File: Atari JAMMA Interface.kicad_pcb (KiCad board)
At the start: 2 copper layers, 112.2 x 74.8 mm, 45 parts, among them P1 10K, U1 LM386, U2 DIP-14_W7.62mm, U3 MC34063AP, U4 74LS04

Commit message: minor tweaks to inductor
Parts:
- moved L1 0.09 mm to (109.6, 125.6)
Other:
- board text added: "1A"
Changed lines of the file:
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@@
 	(footprint "Inductor_THT:L_Radial_D6.0mm_P4.00mm"
 		(layer "F.Cu")
-		(at 109.6 125.5)
+		(at 109.6 125.59)
 		(descr "Inductor, Radial series, Radial, pin pitch=4.00mm, diameter=6.0mm, height=4.6mm, http://www.abracon.com/Magnetics/radial/AIUR-07.pdf")
 		(tags "Inductor Radial series Radial pin pitch 4.00mm  diameter 6.0mm height 4.6mm")
@@
 		)
 	)
+	(gr_text "1A"
+		(at 111.6 131.275538 0)
+		(layer "F.SilkS")
+		(effects
+			(font
+				(size 0.72 0.72)
+				(thickness 0.108)
+			)
+		)
+	)
 	(gr_text "1P B4"
 		(at 120.191885 91.8 90)
@@
 	)
 	(segment
-		(start 111 125.987872)
-		(end 111 114.2)
-		(width 0.2)
-		(layer "F.Cu")
-		(net 9)
-	)
-	(segment
-		(start 192.4 134.4)
-		(end 119.412128 134.4)
-		(width 0.2)
-		(layer "F.Cu")
-		(net 9)
-	)
-	(segment
-		(start 113.6 99.565685)
-		(end 113.6 98.8)
+		(start 115.8 96.6)
+		(end 115.8 93.4)
 		(width 0.2)
 		(layer "F.Cu")
@@
 	)
 	(segment
-		(start 176.82 122.58)
-		(end 179.59 125.35)
+		(start 108.4 111.6)
+		(end 108.4 104.765686)
 		(width 0.2)
 		(layer "F.Cu")
@@
 	)
 	(segment
-		(start 108.4 111.6)
-		(end 108.4 104.765686)
+		(start 176.82 122.58)
+		(end 179.59 125.35)
 		(width 0.2)
 		(layer "F.Cu")
@@
 	)
 	(segment
-		(start 116.4 92.8)
-		(end 122.430112 92.8)
+		(start 122.430112 92.8)
+		(end 128.428249 86.801863)
 		(width 0.2)
 		(layer "F.Cu")
@@
 	)
 	(segment
-		(start 113.6 98.8)
-		(end 115.8 96.6)
+		(start 113.6 99.565685)
+		(end 113.6 98.8)
 		(width 0.2)
 		(layer "F.Cu")
@@
 	)
 	(segment
-		(start 108.4 104.765686)
-		(end 113.6 99.565685)
+		(start 111 126.365685)
+		(end 111 114.2)
 		(width 0.2)
 		(layer "F.Cu")
@@
 	)
 	(segment
+		(start 113.6 98.8)
+		(end 115.8 96.6)
+		(width 0.2)
+		(layer "F.Cu")
+		(net 9)
+	)
+	(segment
+		(start 192.4 134.4)
+		(end 119.034314 134.4)
+		(width 0.2)
+		(layer "F.Cu")
+		(net 9)
+	)
+	(segment
 		(start 192.682856 134.4)
 		(end 197.282856 129.8)
@@
 	)
 	(segment
-		(start 128.428249 86.801863)
-		(end 128.428249 69.766603)
+		(start 116.4 92.8)
+		(end 122.430112 92.8)
 		(width 0.2)
 		(layer "F.Cu")
@@
 	)
 	(segment
-		(start 115.8 96.6)
-		(end 115.8 93.4)
+		(start 108.4 104.765686)
+		(end 113.6 99.565685)
 		(width 0.2)
 		(layer "F.Cu")
@@
 	)
 	(segment
-		(start 122.430112 92.8)
-		(end 128.428249 86.801863)
+		(start 128.428249 86.801863)
+		(end 128.428249 69.766603)
 		(width 0.2)
 		(layer "F.Cu")
@@
 	)
 	(segment
-		(start 119.412128 134.4)
-		(end 111 125.987872)
+		(start 119.034314 134.4)
+		(end 111 126.365685)
 		(width 0.2)
 		(layer "F.Cu")
@@
 	)
 	(segment
-		(start 111.6 121.6)
-		(end 111.6 126)
+		(start 111.6 117.2)
+		(end 111.54088 117.25912)
 		(width 0.2)
 		(layer "F.Cu")
@@
 	)
 	(segment
-		(start 131.898249 69.276603)
-		(end 131.898249 73.176603)
+		(start 166.95 134)
+		(end 167.2 133.75)
 		(width 0.2)
 		(layer "F.Cu")
@@
 	)
 	(segment
-		(start 193.2 129.8)
-		(end 193.454285 129.8)
+		(start 131.898249 69.276603)
+		(end 131.898249 73.176603)
 		(width 0.2)
 		(layer "F.Cu")
@@
 	)
 	(segment
-		(start 111.54088 121.54088)
-		(end 111.6 121.6)
+		(start 193.2 129.8)
+		(end 193.454285 129.8)
 		(width 0.2)
 		(layer "F.Cu")
@@
 	)
 	(segment
-		(start 119.6 134)
-		(end 166.95 134)
-		(width 0.2)
-		(layer "F.Cu")
-		(net 10)
-	)
-	(segment
-		(start 111.6 126)
-		(end 119.6 134)
+		(start 111.54088 121.54088)
+		(end 111.6 121.6)
 		(width 0.2)
 		(layer "F.Cu")
@@
 	)
 	(segment
+		(start 131.898249 73.176603)
+		(end 130.628249 74.446603)
+		(width 0.2)
+		(layer "F.Cu")
+		(net 10)
+	)
+	(segment
 		(start 111.54088 117.25912)
 		(end 111.54088 121.54088)
@@
 	)
 	(segment
-		(start 131.898249 73.176603)
-		(end 130.628249 74.446603)
+		(start 119.2 134)
+		(end 166.95 134)
 		(width 0.2)
 		(layer "F.Cu")
@@
 	)
 	(segment
-		(start 112.2 109.2)
-		(end 111.6 109.2)
+		(start 111.6 121.6)
+		(end 111.6 126.4)
 		(width 0.2)
 		(layer "F.Cu")
@@
 	)
 	(segment
-		(start 111.6 117.2)
-		(end 111.54088 117.25912)
+		(start 112.2 109.2)
+		(end 111.6 109.2)
 		(width 0.2)
 		(layer "F.Cu")
@@
 	)
 	(segment
-		(start 191.2 131.8)
-		(end 193.2 129.8)
+		(start 111.6 126.4)
+		(end 119.2 134)
 		(width 0.2)
 		(layer "F.Cu")
@@
 	)
 	(segment
-		(start 166.95 134)
-		(end 167.2 133.75)
+		(start 191.2 131.8)
+		(end 193.2 129.8)
 		(width 0.2)
 		(layer "F.Cu")
@@
 	)
 	(segment
-		(start 168.033704 133)
-		(end 167 133)
+		(start 119.4 133.6)
+		(end 112.2 126.4)
 		(width 0.2)
 		(layer "F.Cu")
@@
 	)
 	(segment
-		(start 167 133)
-		(end 166.4 133.6)
-		(width 0.2)
-		(layer "F.Cu")
-		(net 11)
-	)
-	(segment
-		(start 112.2 126)
-		(end 112.2 117.75912)
+		(start 112.2 117.75912)
+		(end 112.19088 117.75)
 		(width 0.2)
 		(layer "F.Cu")
@@
 	)
 	(segment
-		(start 166.4 133.6)
-		(end 119.8 133.6)
-		(width 0.2)
-		(layer "F.Cu")
-		(net 11)
-	)
-	(segment
-		(start 119.8 133.6)
-		(end 112.2 126)
+		(start 168.033704 133)
+		(end 167 133)
 		(width 0.2)
 		(layer "F.Cu")
@@
 	)
 	(segment
-		(start 112.2 117.75912)
-		(end 112.19088 117.75)
+		(start 112.2 126.4)
+		(end 112.2 117.75912)
 		(width 0.2)
 		(layer "F.Cu")
@@
 	)
 	(segment
+		(start 166.4 133.6)
+		(end 119.4 133.6)
+		(width 0.2)
+		(layer "F.Cu")
+		(net 11)
+	)
+	(segment
 		(start 187.8 131.4)
 		(end 189.4 129.8)
@@
 	)
 	(segment
+		(start 167 133)
+		(end 166.4 133.6)
+		(width 0.2)
+		(layer "F.Cu")
+		(net 11)
+	)
+	(segment
 		(start 174.28 130.2)
 		(end 175.48 131.4)
@@
 	)
 	(segment
-		(start 115.95 123.25)
-		(end 113.7 125.5)
-		(width 0.6)
-		(layer "F.Cu")
-		(net 52)
-	)
-	(segment
-		(start 126 128.960108)
-		(end 120.289892 123.25)
+		(start 126 130)
+		(end 126 128.4)
 		(width 0.6)
 		(layer "F.Cu")
@@
 	)
 	(segment
-		(start 126 130)
-		(end 126 128.960108)
+		(start 113.7 125.5)
+		(end 113.6 125.5)
 		(width 0.6)
 		(layer "F.Cu")
@@
 	)
 	(segment
-		(start 113.7 125.5)
-		(end 113.6 125.5)
+		(start 120.85 123.25)
+		(end 115.95 123.25)
 		(width 0.6)
 		(layer "F.Cu")
@@
 	)
 	(segment
-		(start 120.289892 123.25)
-		(end 115.95 123.25)
+		(start 126 128.4)
+		(end 120.85 123.25)
 		(width 0.6)
 		(layer "F.Cu")
@@
 		(width 0.6)
 		(layer "F.Cu")
+		(net 52)
+	)
+	(segment
+		(start 115.95 123.25)
+		(end 113.7 125.5)
+		(width 0.6)
+		(layer "F.Cu")

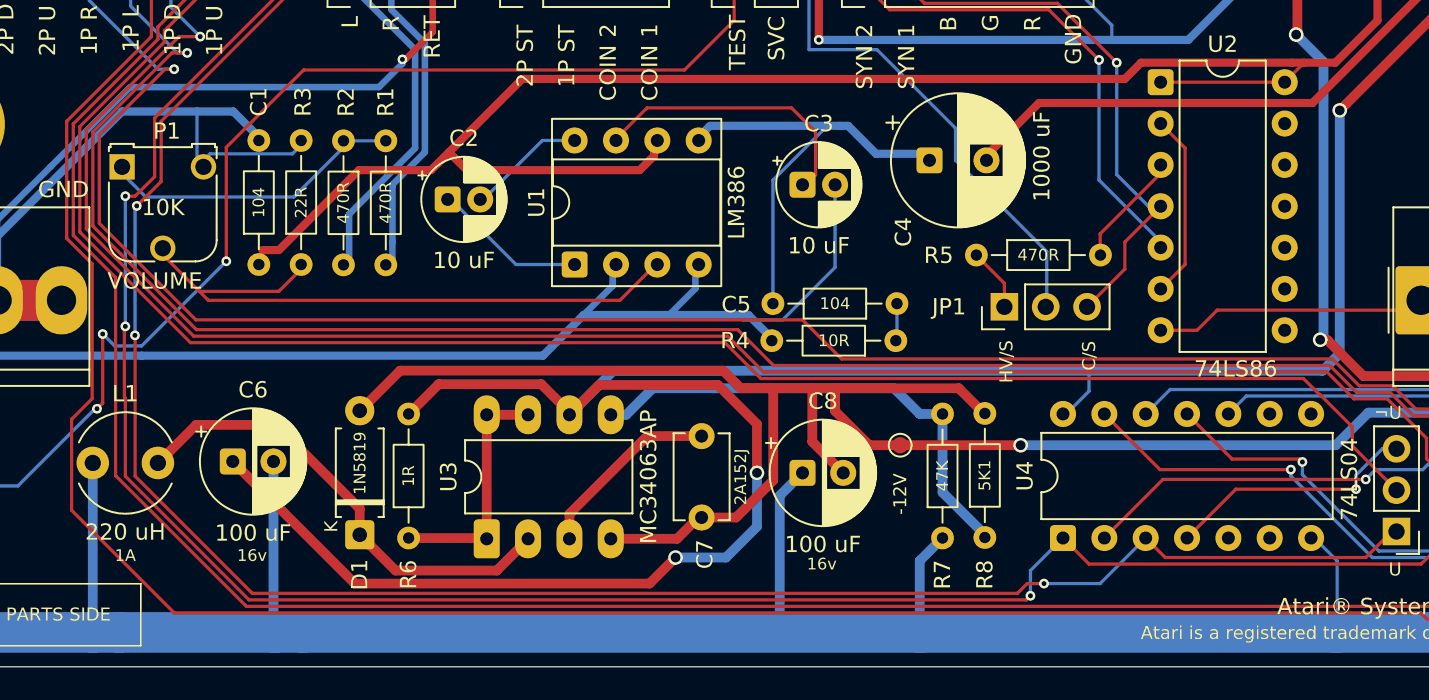
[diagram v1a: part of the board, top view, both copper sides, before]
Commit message: slight tweaks to layout and silkscreen
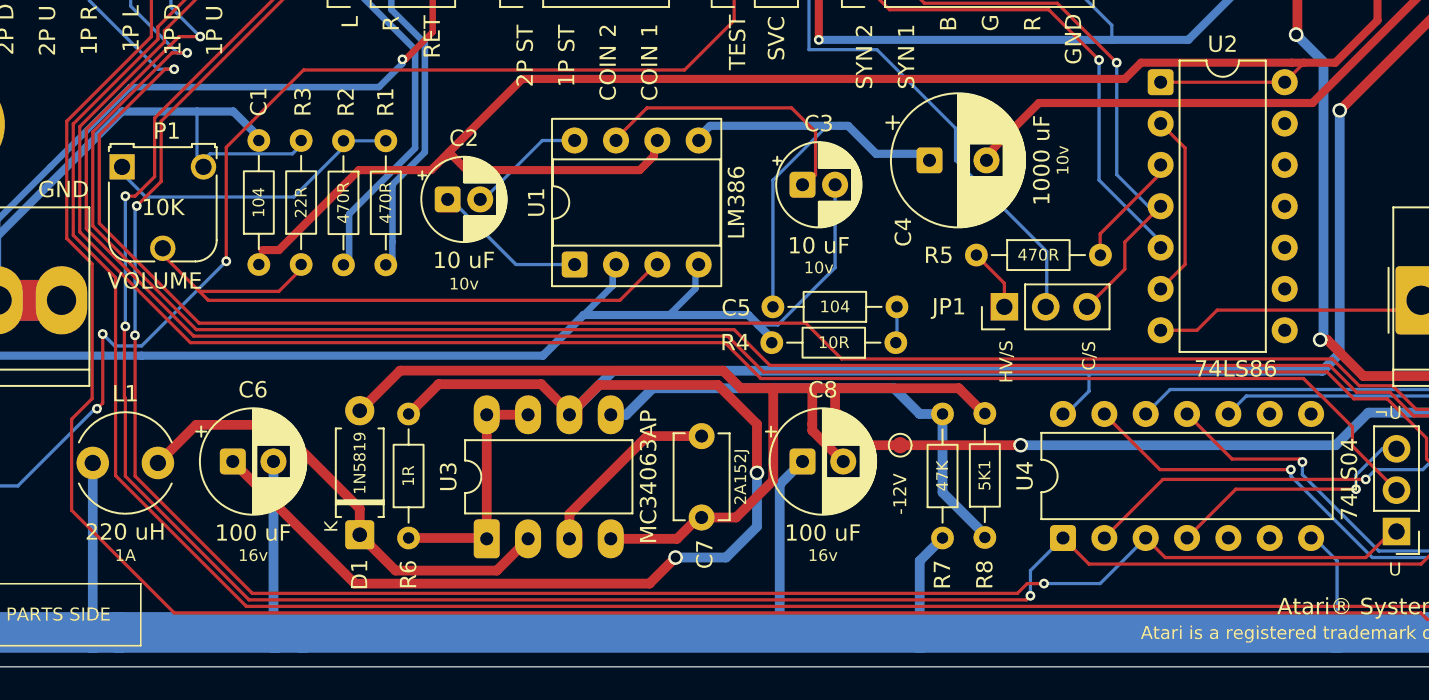
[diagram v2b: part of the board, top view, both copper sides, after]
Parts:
- moved C8 0.70 mm to (153.2, 125.5)
- moved C5 0.20 mm to (159.0, 116.0)
- moved R4 0.12 mm to (158.9, 118.2)
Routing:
- net -12V: track 151.6 -> 150.9 mm
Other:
- board text added: "10v"

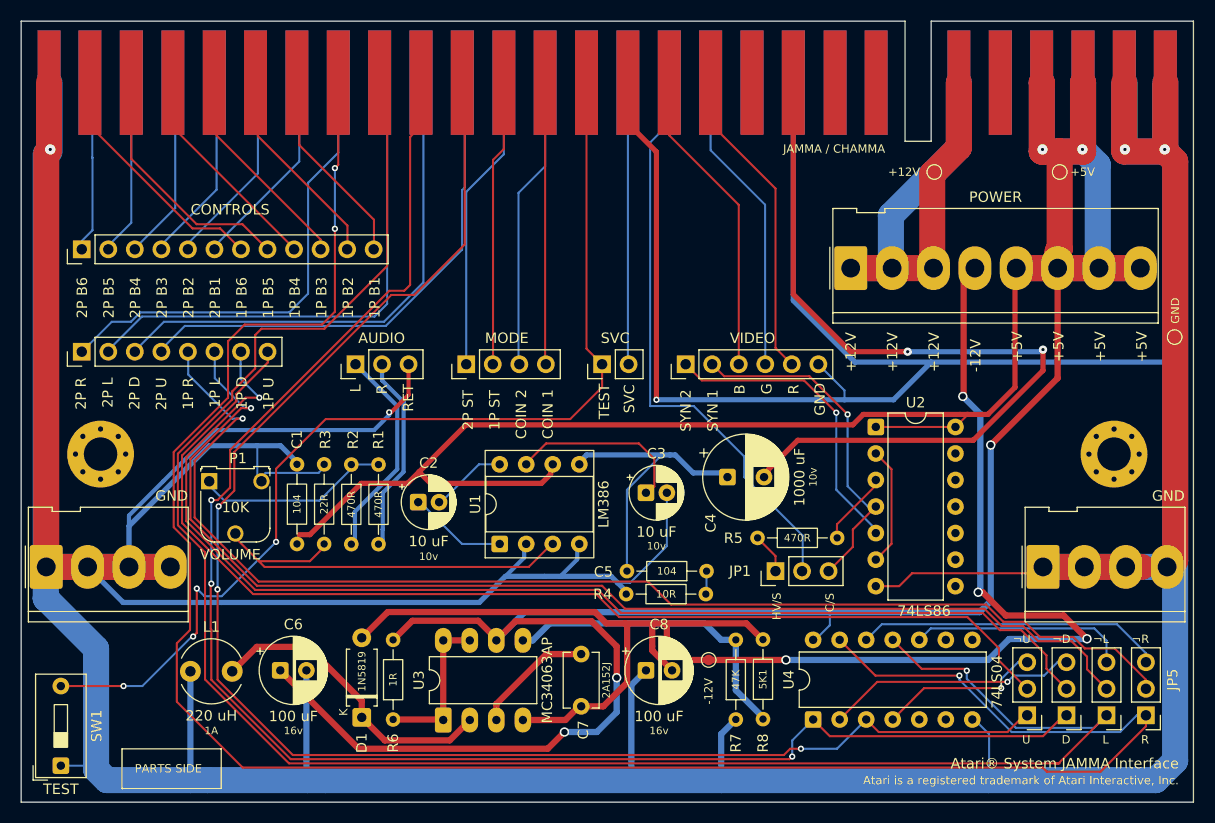
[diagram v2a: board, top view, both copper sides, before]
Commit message: silksreen alignment
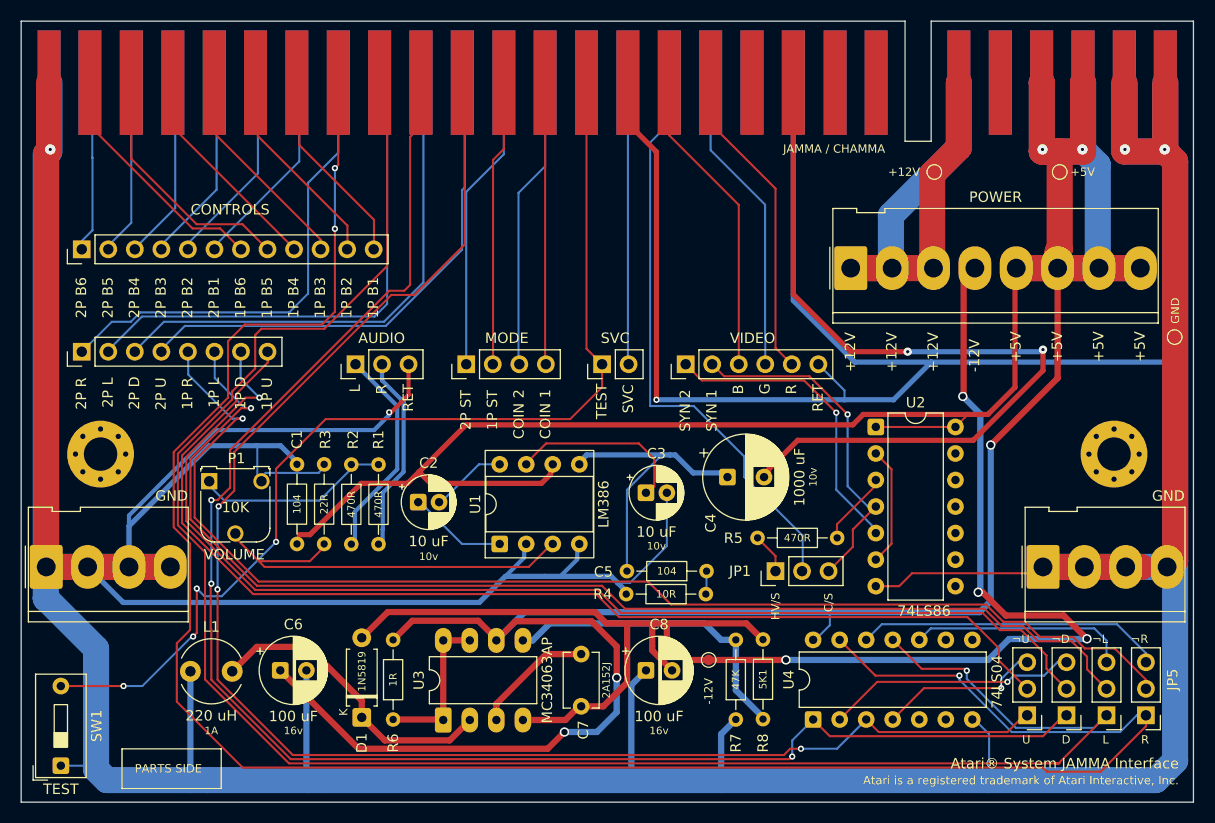
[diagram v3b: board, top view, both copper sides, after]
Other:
- board text removed: "GND"
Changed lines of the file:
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@@
 		(tags "Potentiometer Trimmer RM-065")
 		(property "Reference" "P1"
-			(at 2.753743 -2.191821 0)
+			(at 2.6 -2.191821 0)
 			(layer "F.SilkS")
 			(effects
@@
 		(tags "Through hole pin header THT 1x03 2.54mm single row")
 		(property "Reference" "HV/S"
-			(at -3.368286 0.121002 90)
+			(at -3.368286 0 90)
 			(layer "F.SilkS")
 			(effects
@@
 	)
 	(gr_text "SYN 2"
-		(at 157.6 102.652734 90)
+		(at 157.5395 102.652734 90)
 		(layer "F.SilkS")
 		(effects
@@
 	)
 	(gr_text "C/S"
-		(at 170.8 119.006381 90)
+		(at 170.68 119.006381 90)
 		(layer "F.SilkS")
 		(effects
@@
 	)
 	(gr_text "L"
-		(at 126 98.890829 90)
+		(at 125.9395 98.890829 90)
 		(layer "F.SilkS")
 		(effects
@@
 	)
 	(gr_text "+5V"
-		(at 193.282901 96 90)
+		(at 193.1395 96 90)
 		(layer "F.SilkS")
 		(effects
@@
 	)
 	(gr_text "2P ST"
-		(at 136.752167 102.509877 90)
+		(at 136.5395 102.509877 90)
 		(layer "F.SilkS")
 		(effects
@@
 	)
 	(gr_text "G"
-		(at 165.34278 99.081305 90)
+		(at 165.1595 99.081305 90)
 		(layer "F.SilkS")
 		(effects
@@
 	)
 	(gr_text "1P B5"
-		(at 117.646431 91.8 90)
+		(at 117.5195 91.8 90)
 		(layer "F.SilkS")
 		(effects
@@
 	)
 	(gr_text "2P B5"
-		(at 102.373704 91.8 90)
+		(at 102.2795 91.8 90)
 		(layer "F.SilkS")
 		(effects
@@
 	)
 	(gr_text "¬L"
-		(at 195.985647 122.974989 0)
+		(at 195.898571 122.974989 0)
 		(layer "F.SilkS")
 		(effects
@@
 		)
 	)
-	(gr_text "GND"
-		(at 170.437318 101.128924 90)
+	(gr_text "RET"
+		(at 170.2395 100.747972 90)
 		(layer "F.SilkS")
 		(effects
@@
 	)
 	(gr_text "SVC"
-		(at 152.195045 100.890829 90)
+		(at 152.0795 100.890829 90)
 		(layer "F.SilkS")
 		(effects
@@
 	)
 	(gr_text "2P B4"
-		(at 104.919158 91.8 90)
+		(at 104.8195 91.8 90)
 		(layer "F.SilkS")
 		(effects
@@
 	)
 	(gr_text "¬D"
-		(at 192.080885 122.974989 0)
+		(at 191.993809 122.974989 0)
 		(layer "F.SilkS")
 		(effects
@@
 	)
 	(gr_text "B"
-		(at 162.761853 99.081305 90)
+		(at 162.6195 99.081305 90)
 		(layer "F.SilkS")
 		(effects
@@
 	)
 	(gr_text "2P B2"
-		(at 110.010067 91.8 90)
+		(at 109.8995 91.8 90)
 		(layer "F.SilkS")
 		(effects
@@
 	)
 	(gr_text "+5V"
-		(at 201.236061 96 90)
+		(at 201.0595 96 90)
 		(layer "F.SilkS")
 		(effects
@@
 	)
 	(gr_text "+12V"
-		(at 181.35316 96.952381 90)
+		(at 181.2595 96.952381 90)
 		(layer "F.SilkS")
 		(effects
@@
 	)
 	(gr_text "1P U"
-		(at 117.669816 100.6 90)
+		(at 117.5195 100.6 90)
 		(layer "F.SilkS")
 		(effects
@@
 	)
 	(gr_text "1P B4"
-		(at 120.191885 91.8 90)
+		(at 120.0595 91.8 90)
 		(layer "F.SilkS")
 		(effects
@@
 	)
 	(gr_text "2P B3"
-		(at 107.464613 91.8 90)
+		(at 107.3595 91.8 90)
 		(layer "F.SilkS")
 		(effects
@@
 	)
 	(gr_text "¬R"
-		(at 199.680885 122.974989 0)
+		(at 199.593809 122.974989 0)
 		(layer "F.SilkS")
 		(effects
@@
 	)
 	(gr_text "+5V"
-		(at 197.259481 96 90)
+		(at 197.0995 96 90)
 		(layer "F.SilkS")
 		(effects
@@
 	)
 	(gr_text "1P D"
-		(at 115.104317 100.552381 90)
+		(at 114.9795 100.552381 90)
 		(layer "F.SilkS")
 		(effects
@@
 	)
 	(gr_text "SYN 1"
-		(at 160.180927 102.652734 90)
+		(at 160.0795 102.652734 90)
 		(layer "F.SilkS")
 		(effects
@@
 	)
 	(gr_text "R"
-		(at 167.923706 99.081305 90)
+		(at 167.6995 99.081305 90)
 		(layer "F.SilkS")
 		(effects
@@
 	)
 	(gr_text "TEST"
-		(at 149.8 101.462258 90)
+		(at 149.5395 101.462258 90)
 		(layer "F.SilkS")
 		(effects
@@
 	)
 	(gr_text "1P B3"
-		(at 122.73734 91.8 90)
+		(at 122.5995 91.8 90)
 		(layer "F.SilkS")
 		(effects
@@
 	)
 	(gr_text "RET"
-		(at 131.040618 100.747972 90)
+		(at 131.0195 100.747972 90)
 		(layer "F.SilkS")
 		(effects
@@
 	)
 	(gr_text "2P L"
-		(at 102.276823 100.361905 90)
+		(at 102.2795 100.361905 90)
 		(layer "F.SilkS")
 		(effects
@@
 	)
 	(gr_text "2P U"
-		(at 107.407821 100.6 90)
+		(at 107.3595 100.6 90)
 		(layer "F.SilkS")
 		(effects
@@
 	)
 	(gr_text "1P ST"
-		(at 139.301445 102.509877 90)
+		(at 139.0795 102.509877 90)
 		(layer "F.SilkS")
 		(effects
@@
 	)
 	(gr_text "+12V"
-		(at 177.37658 96.952381 90)
+		(at 177.2995 96.952381 90)
 		(layer "F.SilkS")
 		(effects
@@
 	)
 	(gr_text "2P B1"
-		(at 112.555522 91.8 90)
+		(at 112.4395 91.8 90)
 		(layer "F.SilkS")
 		(effects
@@
 	)
 	(gr_text "1P B1"
-		(at 127.828249 91.8 90)
+		(at 127.6795 91.8 90)
 		(layer "F.SilkS")
 		(effects
@@
 	)
 	(gr_text "2P B6"
-		(at 99.828249 91.8 90)
+		(at 99.7395 91.8 90)
 		(layer "F.SilkS")
 		(effects
@@
 	)
 	(gr_text "COIN 2"
-		(at 141.850722 103.367019 90)
+		(at 141.6195 103.367019 90)
 		(layer "F.SilkS")
 		(effects
@@
 	)
 	(gr_text "1P L"
-		(at 112.538818 100.361905 90)
+		(at 112.4395 100.361905 90)
 		(layer "F.SilkS")
 		(effects
@@
 	)
 	(gr_text "COIN 1"
-		(at 144.4 103.367019 90)
+		(at 144.1595 103.367019 90)
 		(layer "F.SilkS")
 		(effects
@@
 	)
 	(gr_text "+5V"
-		(at 189.306321 96 90)
+		(at 189.1795 96 90)
 		(layer "F.SilkS")
 		(effects
@@
 	)
 	(gr_text "R"
-		(at 128.520309 99.081305 90)
+		(at 128.4795 99.081305 90)
 		(layer "F.SilkS")
 		(effects
@@
 	)
 	(gr_text "+12V"
-		(at 173.4 96.952381 90)
+		(at 173.3395 96.952381 90)
 		(layer "F.SilkS")
 		(effects
@@
 	)
 	(gr_text "VOLUME"
-		(at 110.5 115 0)
+		(at 110.870238 115 0)
 		(layer "F.SilkS")
 		(effects
@@
 	)
 	(gr_text "2P D"
-		(at 104.842322 100.552381 90)
+		(at 104.8195 100.552381 90)
 		(layer "F.SilkS")
 		(effects
@@
 	)
 	(gr_text "1P R"
-		(at 109.973319 100.552381 90)
+		(at 109.8995 100.552381 90)
 		(layer "F.SilkS")
 		(effects
@@
 	)
 	(gr_text "-12V"
-		(at 185.32974 96.952381 90)
+		(at 185.2195 96.952381 90)
 		(layer "F.SilkS")
 		(effects
@@
 	)
 	(gr_text "¬U"
-		(at 188.2966 122.974989 0)
+		(at 188.209524 122.974989 0)
 		(layer "F.SilkS")
 		(effects
@@
 	)
 	(gr_text "1P B2"
-		(at 125.282794 91.8 90)
+		(at 125.1395 91.8 90)
 		(layer "F.SilkS")
 		(effects
@@
 	)
 	(gr_text "1P B6"
-		(at 115.100976 91.8 90)
+		(at 114.9795 91.8 90)
 		(layer "F.SilkS")
 		(effects
@@
 	)
 	(gr_text "2P R"
-		(at 99.711324 100.552381 90)
+		(at 99.7395 100.552381 90)
 		(layer "F.SilkS")
 		(effects
